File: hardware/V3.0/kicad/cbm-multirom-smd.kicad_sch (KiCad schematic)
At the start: 26 parts, among them Con1 Signal, IC1 SST39SF0x0, IC2 328P(B), IC3 74HCT273, IC4 74HCT1G04, Q1 20MHz

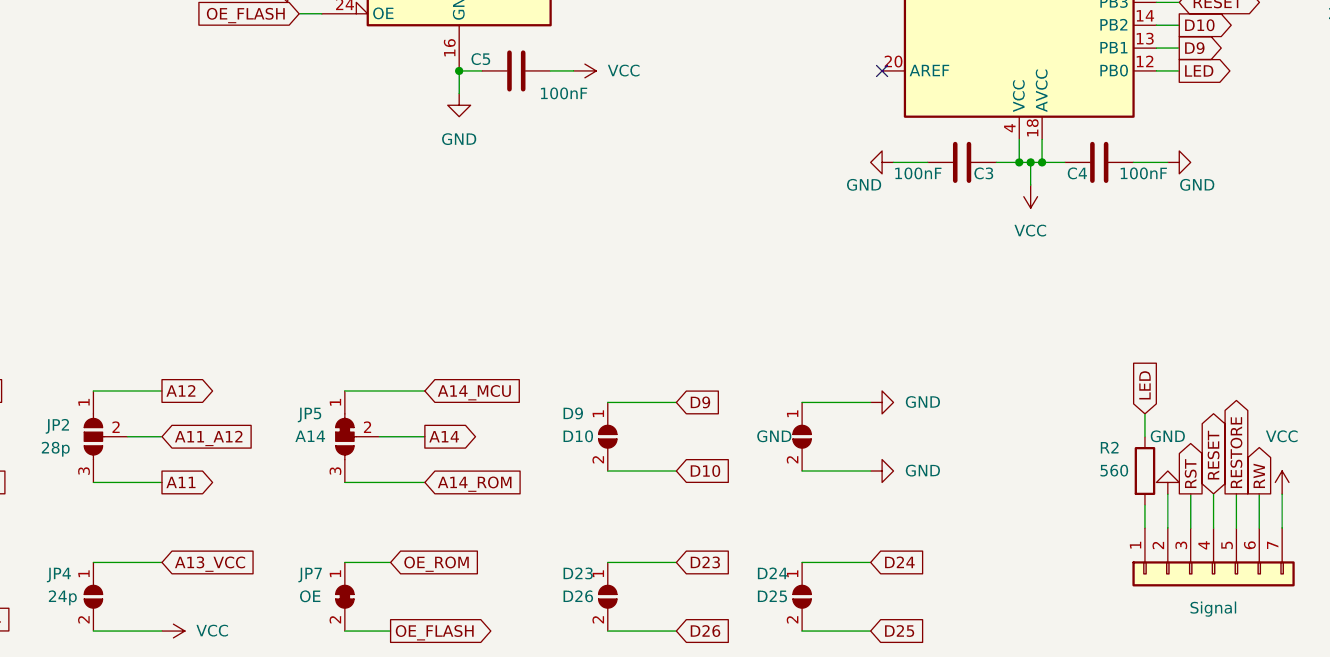
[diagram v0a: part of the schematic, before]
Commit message: V3.0
Changed Jumper setup
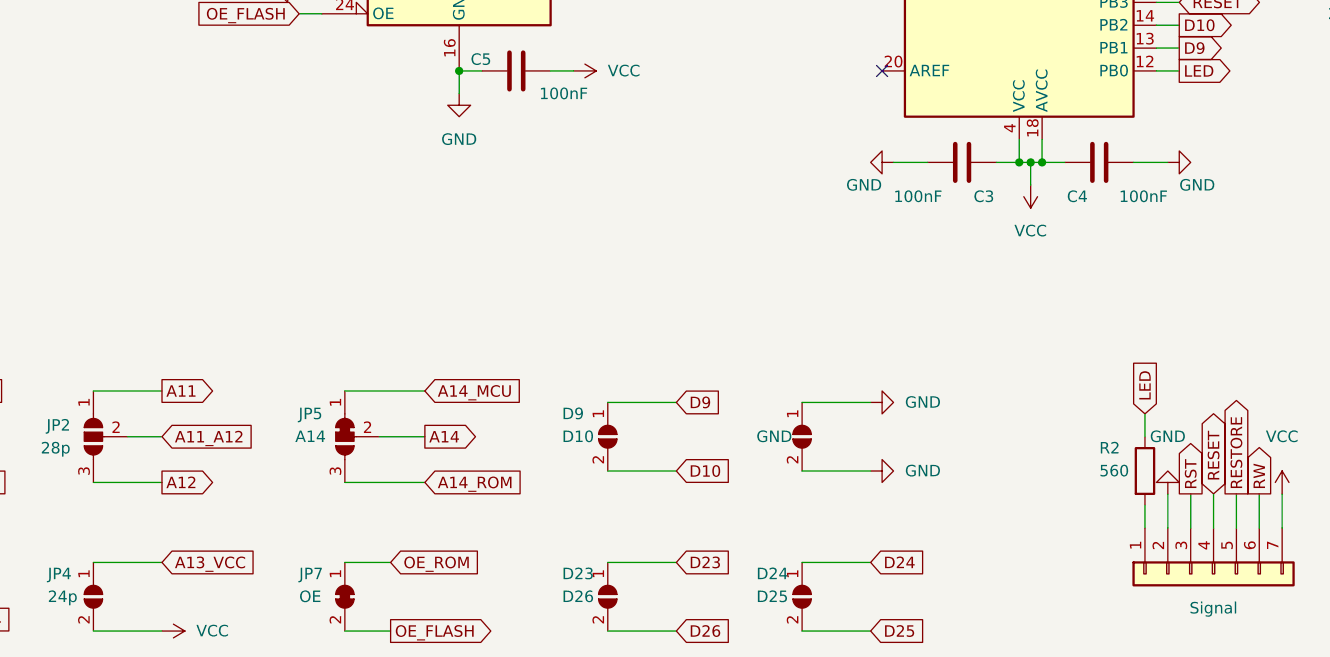
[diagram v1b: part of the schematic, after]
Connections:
- net A11: now also JP2.1 (A); no longer JP2.3 (B)
- net A12: now also JP2.3 (B); no longer JP2.1 (A)
